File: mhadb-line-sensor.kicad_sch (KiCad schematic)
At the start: 84 parts, among them J1 Conn_01x04, J2 TC2030, J4 Conn_01x04_Pin, SW2 SW_Push, SW3 SW_Push, U1 STM32F103C8Tx, U10 QRE1113GR, U11 QRE1113GR, U12 QRE1113GR, U2 QRE1113GR, U3 SN65HVD230, U4 QRE1113GR, U5 QRE1113GR, U6 QRE1113GR, U7 QRE1113GR, U8 QRE1113GR, U9 QRE1113GR, Y1 8M

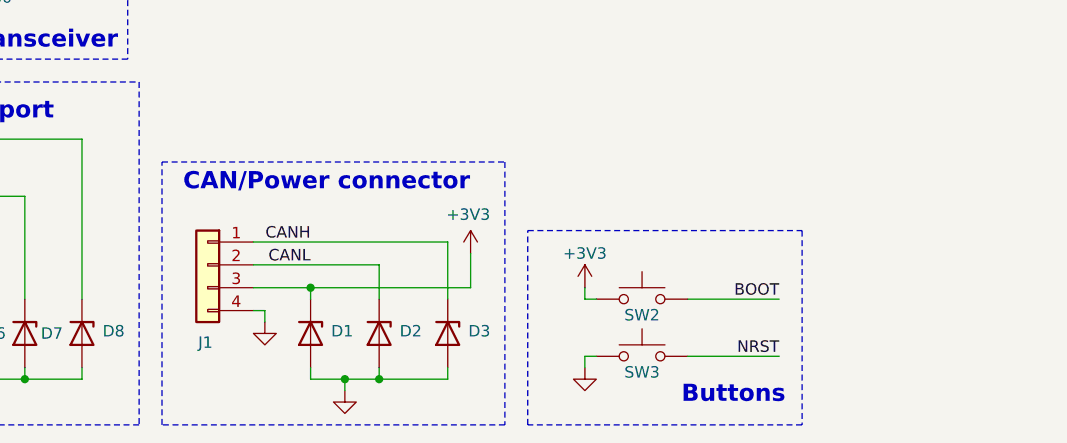
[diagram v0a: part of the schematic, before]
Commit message: schem: add 3v3 input bulk capacitance
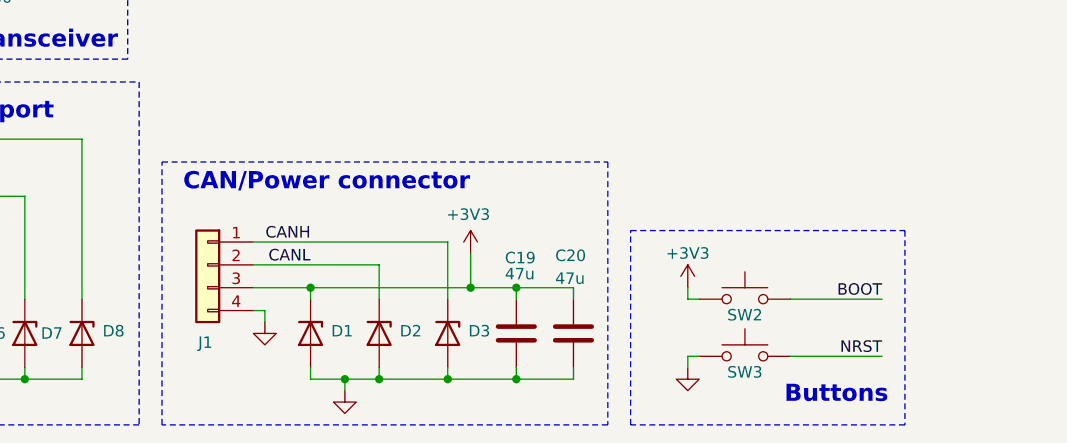
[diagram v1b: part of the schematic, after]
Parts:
- added C19, C20: 47u, Capacitor_SMD:C_1206_3216Metric, symbol Device:C
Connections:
- net +3V3: now also C19.1, C20.1
- net GND: now also C19.2, C20.2
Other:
- moved on the sheet: SW2, SW3

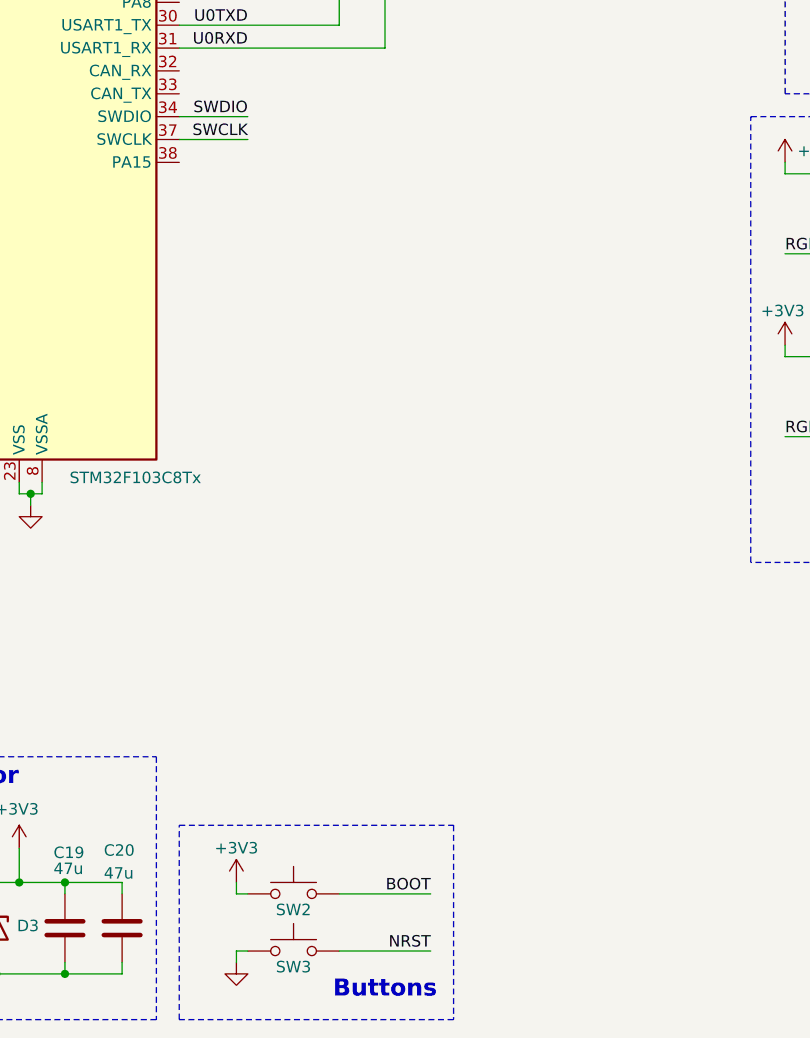
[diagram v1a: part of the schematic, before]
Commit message: schem: add indicator leds
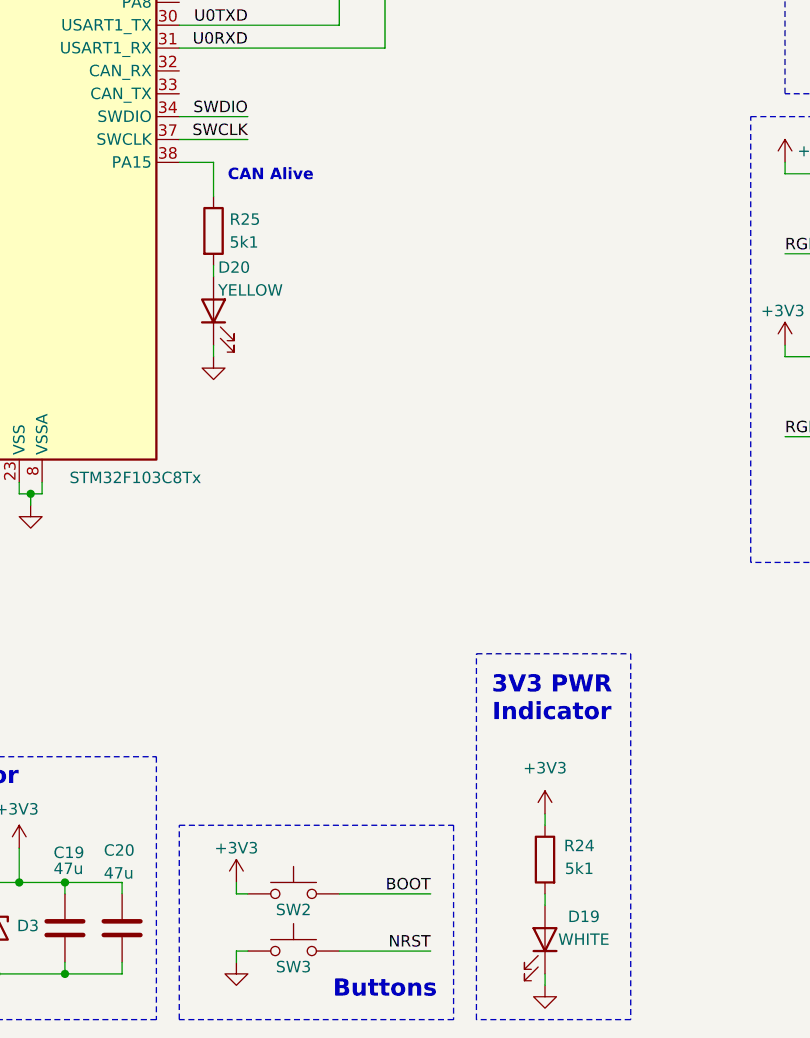
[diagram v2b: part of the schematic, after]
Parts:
- added D19: WHITE, LED_SMD:LED_0603_1608Metric, symbol Device:LED
- added D20: YELLOW, LED_SMD:LED_0805_2012Metric, symbol Device:LED
- added R24, R25: 5k1, Resistor_SMD:R_0402_1005Metric, symbol Device:R
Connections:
- net +3V3: now also R24.1
- net GND: now also D19.1 (K), D20.1 (K)
- net at U1.38 (PA15): now also R25.1
- new net: D20.2 (A), R25.2
- new net: D19.2 (A), R24.2
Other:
- note added: "3V3 PWR Indicator"
- note added: "CAN Alive"

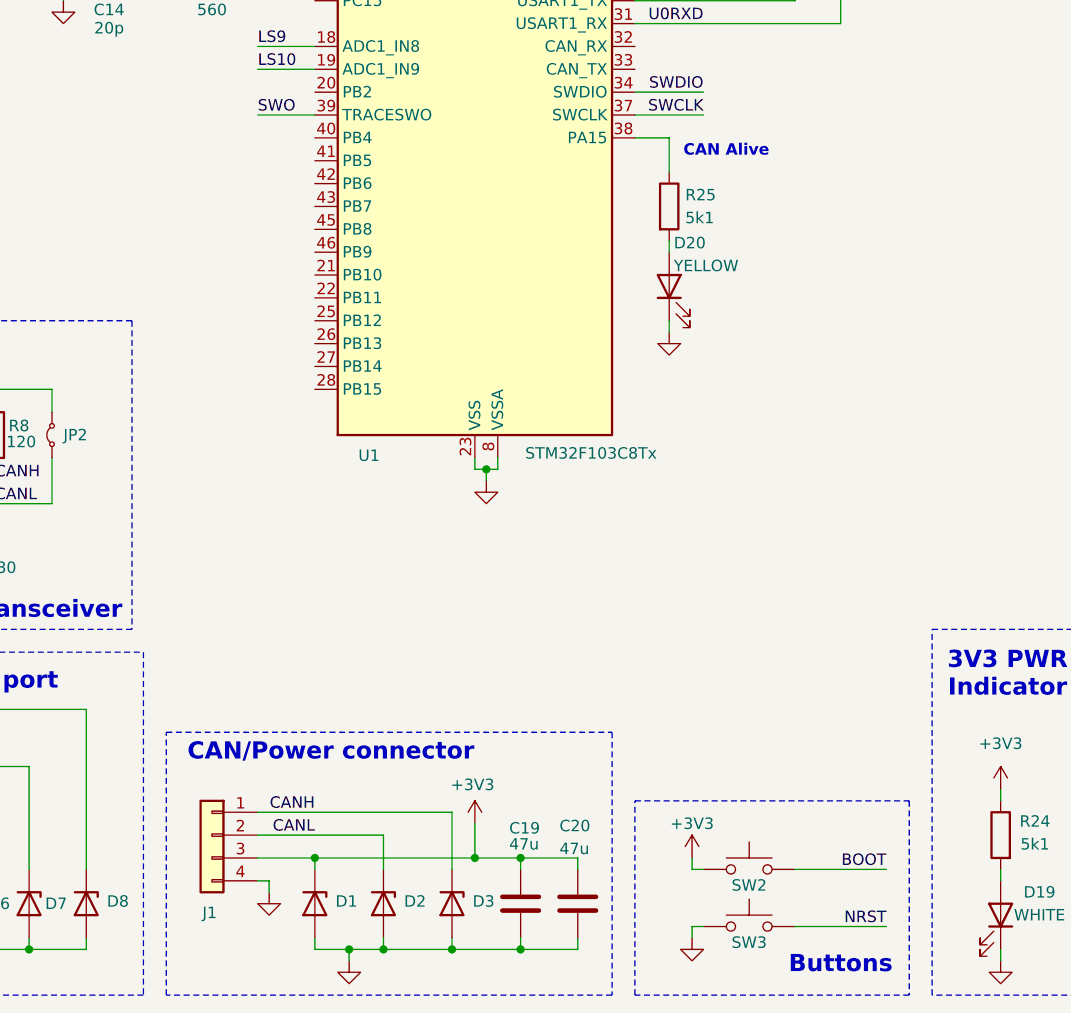
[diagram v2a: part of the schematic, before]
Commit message: schem: add general btns
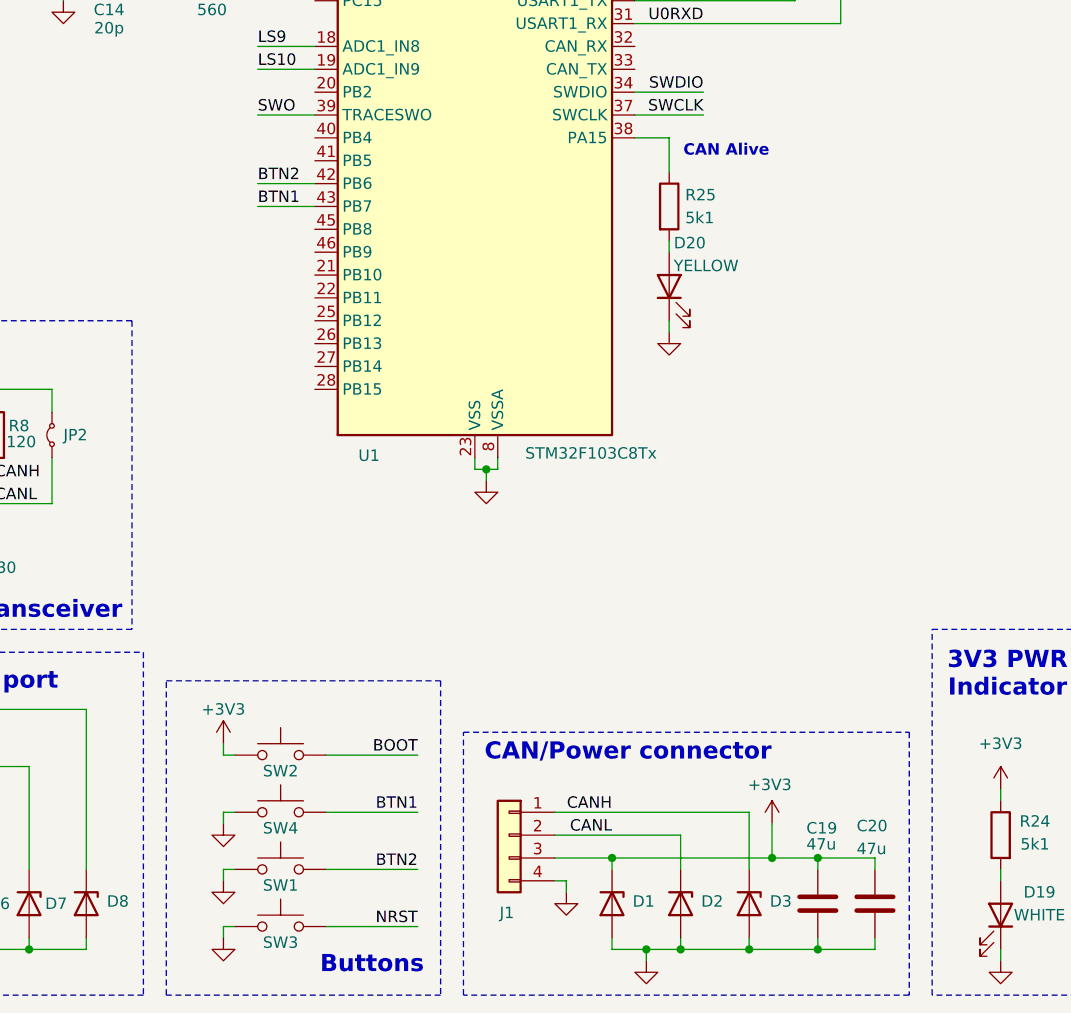
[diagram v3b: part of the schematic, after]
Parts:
- added SW1, SW4: SW_Push, Button_Switch_SMD:SW_SPST_TS-1088-xR020, symbol Switch:SW_Push
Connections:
- net GND: now also SW1.1, SW4.1
- net BTN2: now reaches U1.42 (PB6)
- net BTN2: now also SW1.2
- net BTN1: now reaches U1.43 (PB7)
- net BTN1: now also SW4.2
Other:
- moved on the sheet: C19, C20, D1, D2, D3, J1, SW2, SW3

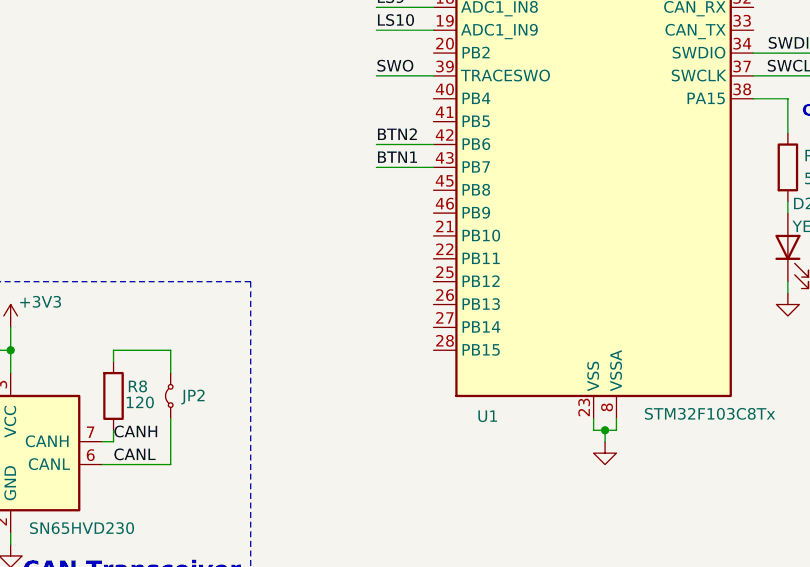
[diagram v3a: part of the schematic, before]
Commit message: schem: connect RGB leds to MCU
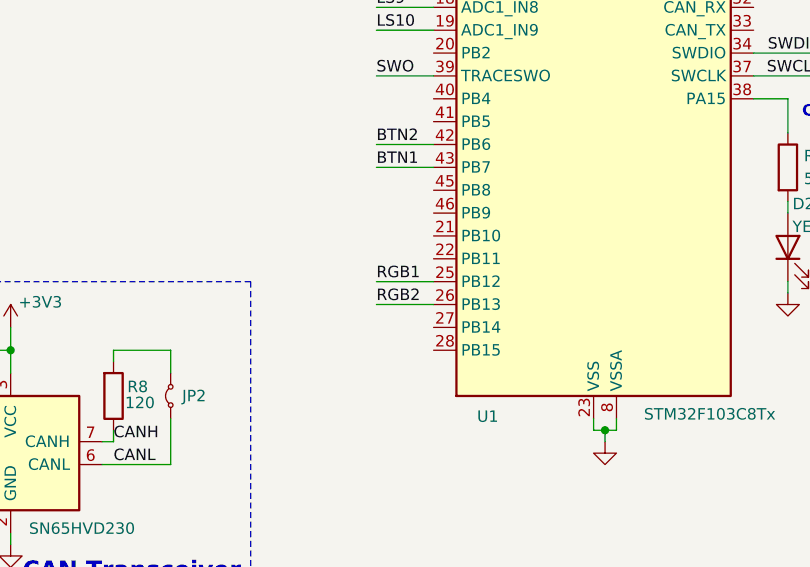
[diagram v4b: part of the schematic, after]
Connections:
- net RGB1: now also U1.25 (PB12)
- net RGB2: now also U1.26 (PB13)
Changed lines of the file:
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@@
+	(wire
+		(pts
+			(xy 81.28 120.65) (xy 87.63 120.65)
+		)
+		(stroke
+			(width 0)
+			(type default)
+		)
+	)
 	(wire
 		(pts
@@
 		(pts
 			(xy 203.2 39.37) (xy 208.28 39.37)
+		)
+		(stroke
+			(width 0)
+			(type default)
+		)
+	)
+	(wire
+		(pts
+			(xy 81.28 123.19) (xy 87.63 123.19)
 		)
 		(stroke
@@
 		)
 	)
+	(label "RGB1"
+		(at 81.28 120.65 0)
+		(effects
+			(font
+				(size 1.27 1.27)
+			)
+			(justify left bottom)
+		)
+	)
 	(label "LS5"
 		(at 204.47 81.28 0)
 		(effects
 			(font
+				(size 1.27 1.27)
+			)
+			(justify left bottom)
+		)
+	)
+	(label "RGB2"
+		(at 81.28 123.19 0)
+		(effects
+			(font

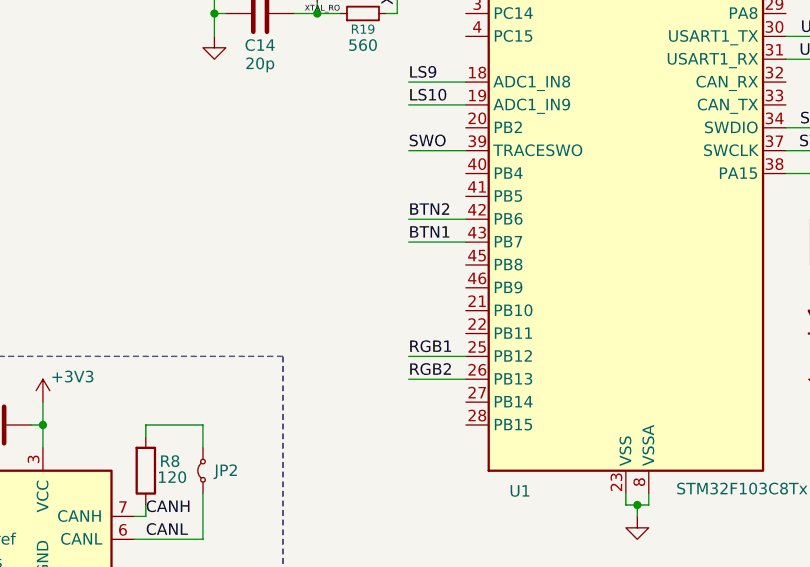
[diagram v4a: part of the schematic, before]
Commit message: schem: add spare GPIOs
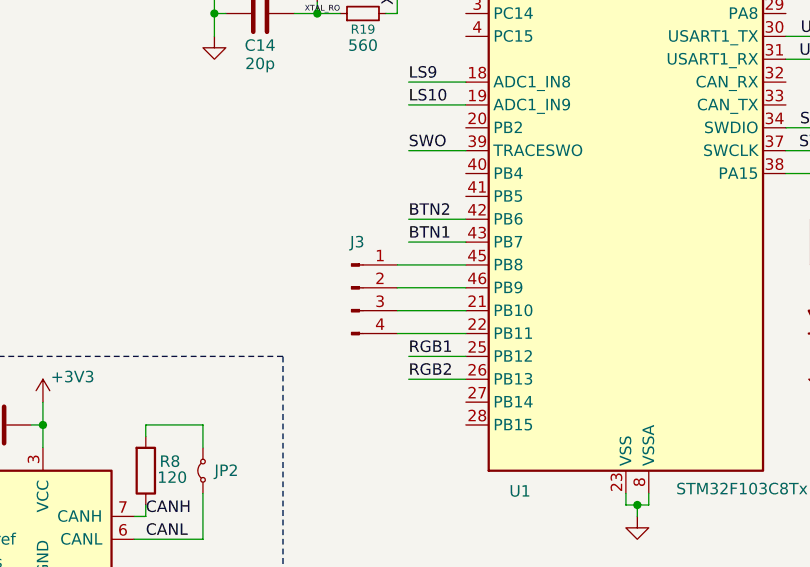
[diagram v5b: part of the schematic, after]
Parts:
- added J3: Conn_01x04_Pin, Connector_PinHeader_2.54mm:PinHeader_1x04_P2.54mm_Vertical, symbol Connector:Conn_01x04_Pin
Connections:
- net at U1.21 (PB10): now also J3.3 (Pin_3)
- net at U1.22 (PB11): now also J3.4 (Pin_4)
- net at U1.45 (PB8): now also J3.1 (Pin_1)
- net at U1.46 (PB9): now also J3.2 (Pin_2)
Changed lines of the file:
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@@
 	(wire
 		(pts
+			(xy 87.63 118.11) (xy 80.01 118.11)
+		)
+		(stroke
+			(width 0)
+			(type default)
+		)
+	)
+	(wire
+		(pts
 			(xy 252.73 139.7) (xy 269.24 139.7)
 		)
@@
 	(wire
 		(pts
+			(xy 87.63 110.49) (xy 80.01 110.49)
+		)
+		(stroke
+			(width 0)
+			(type default)
+		)
+	)
+	(wire
+		(pts
 			(xy 266.7 25.4) (xy 265.43 25.4)
 		)
@@
 	(wire
 		(pts
+			(xy 87.63 113.03) (xy 80.01 113.03)
+		)
+		(stroke
+			(width 0)
+			(type default)
+		)
+	)
+	(wire
+		(pts
 			(xy 146.05 67.31) (xy 146.05 87.63)
 		)
@@
 	(wire
 		(pts
+			(xy 87.63 115.57) (xy 80.01 115.57)
+		)
+		(stroke
+			(width 0)
+			(type default)
+		)
+	)
+	(wire
+		(pts
 			(xy 227.33 130.81) (xy 228.6 130.81)
 		)
@@
 					(unit 1)
 				)
+			)
+		)
+	)
+	(symbol
+		(lib_id "Connector:Conn_01x04_Pin")
+		(at 74.93 113.03 0)
+		(unit 1)
+		(exclude_from_sim no)
+		(in_bom no)
+		(on_board yes)
+		(dnp no)
+		(fields_autoplaced yes)
+		(property "Reference" "J3"
+			(at 75.565 107.95 0)
+			(effects
+				(font
+					(size 1.27 1.27)
+				)
+			)
+		)
+		(property "Value" "Conn_01x04_Pin"
+			(at 72.39 114.3 90)
+			(effects
+				(font
+					(size 1.27 1.27)
+				)
+				(hide yes)
+			)
+		)
+		(property "Footprint" "Connector_PinHeader_2.54mm:PinHeader_1x04_P2.54mm_Vertical"
+			(at 74.93 113.03 0)
+			(effects
+				(font
+					(size 1.27 1.27)
+				)
+				(hide yes)
+			)
+		)
+		(property "Datasheet" "~"
+			(at 74.93 113.03 0)
+			(effects
+				(font
+					(size 1.27 1.27)
+				)
+				(hide yes)
+			)
+		)
+		(property "Description" "Generic connector, single row, 01x04, script generated"
+			(at 74.93 113.03 0)
+			(effects
+				(font
+					(size 1.27 1.27)
+				)
+				(hide yes)
+			)
+		)
+		(pin "4"
+		)
+		(pin "3"
+		)
+		(pin "2"
+		)
+		(pin "1"
+		)
+		(instances
+			(project "mhadb-line-sensor"
+				(path "/dc023b14-f8af-47bb-9afb-84a8ab4a9288"
+					(reference "J3")
+					(unit 1)
+				)
